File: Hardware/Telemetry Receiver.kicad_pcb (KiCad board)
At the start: 4 copper layers, 67 x 23.5 mm, 56 parts, among them IC1 RFX2401C, J1 SMA Connector, J2 USB_C_Receptacle_USB2.0, J3 S4B-XH-A-1, U1 LM1117-3.3, U2 USBLC6-2SC6, U3 STM32L4P5RET6, U4 NRF24L01, U5 36103205S, Y1 Crystal(16MHZ)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

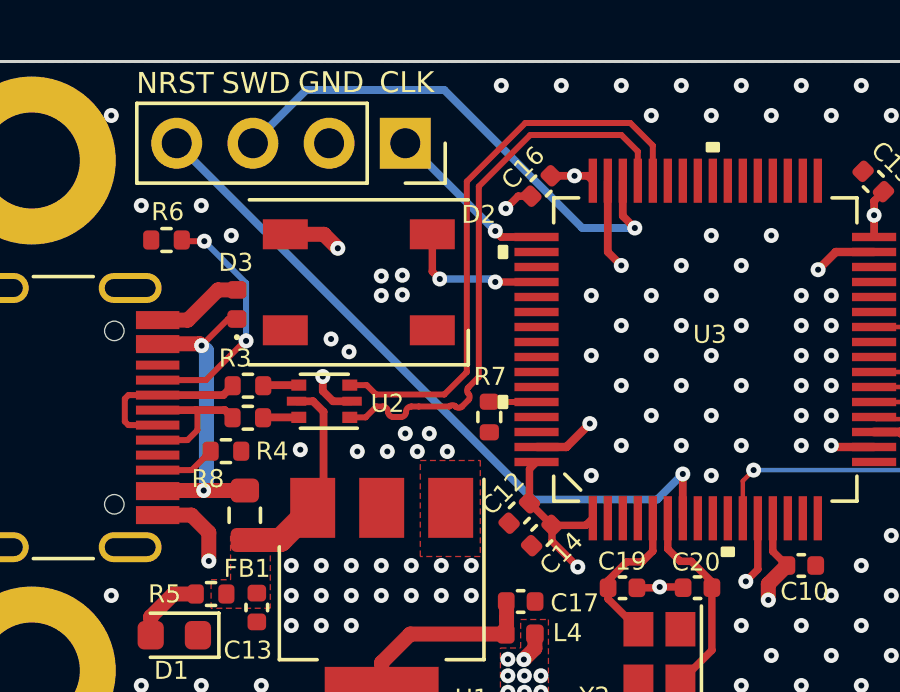
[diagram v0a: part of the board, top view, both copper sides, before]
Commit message: Changed footprint for available one
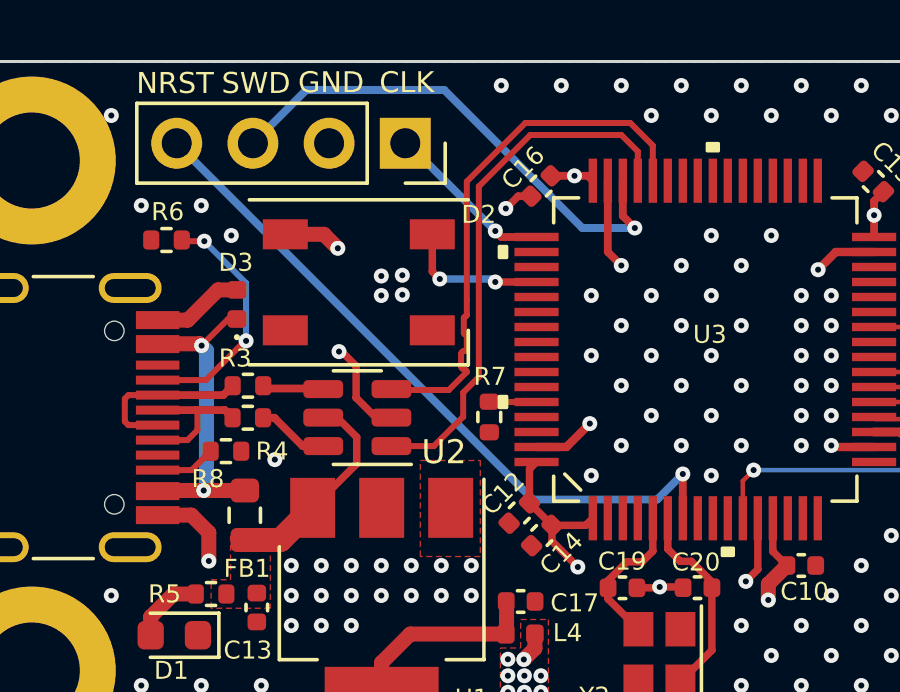
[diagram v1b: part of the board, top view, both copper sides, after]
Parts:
- U2: footprint Package_TO_SOT_SMD:SOT-666 -> Package_TO_SOT_SMD:SOT-23-6
- moved U2 1.23 mm to (95.2, -86.9)
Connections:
- J2 pad S1: (no net) -> unconnected-(J2-PadS1)
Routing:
- net GND: track 44.5 -> 46.2 mm, vias 287 -> 279
- net /USB_D-: track 19.2 -> 17.9 mm
- net Net-(R4-Pad2): track 1.20 -> 2.41 mm
- net /USB_D+: track 19.1 -> 17.9 mm
- net Net-(R3-Pad2): track 1.19 -> 2.13 mm
